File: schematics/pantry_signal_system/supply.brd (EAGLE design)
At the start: 71.1 x 61.3 mm, 58 parts, among them J1 USBASP_PIN, J2 JST-XH254-3P, J3 JST-XH254-2P, J4 JST-XH254-2P, Q1 FDS4935A, Q2 FDS4935A, Q3 FDS4935A, U1 NC7WZ04, U2 AD8544SO-14, U3 FAN73611, U4 FAN73611, U5 MCP1703T-5002E/CB, U6 MCP1703T-5002E/CB, U7 MCP1703T-3302E/CB, U8 FAN73611, U9 ATTINY13SO-8

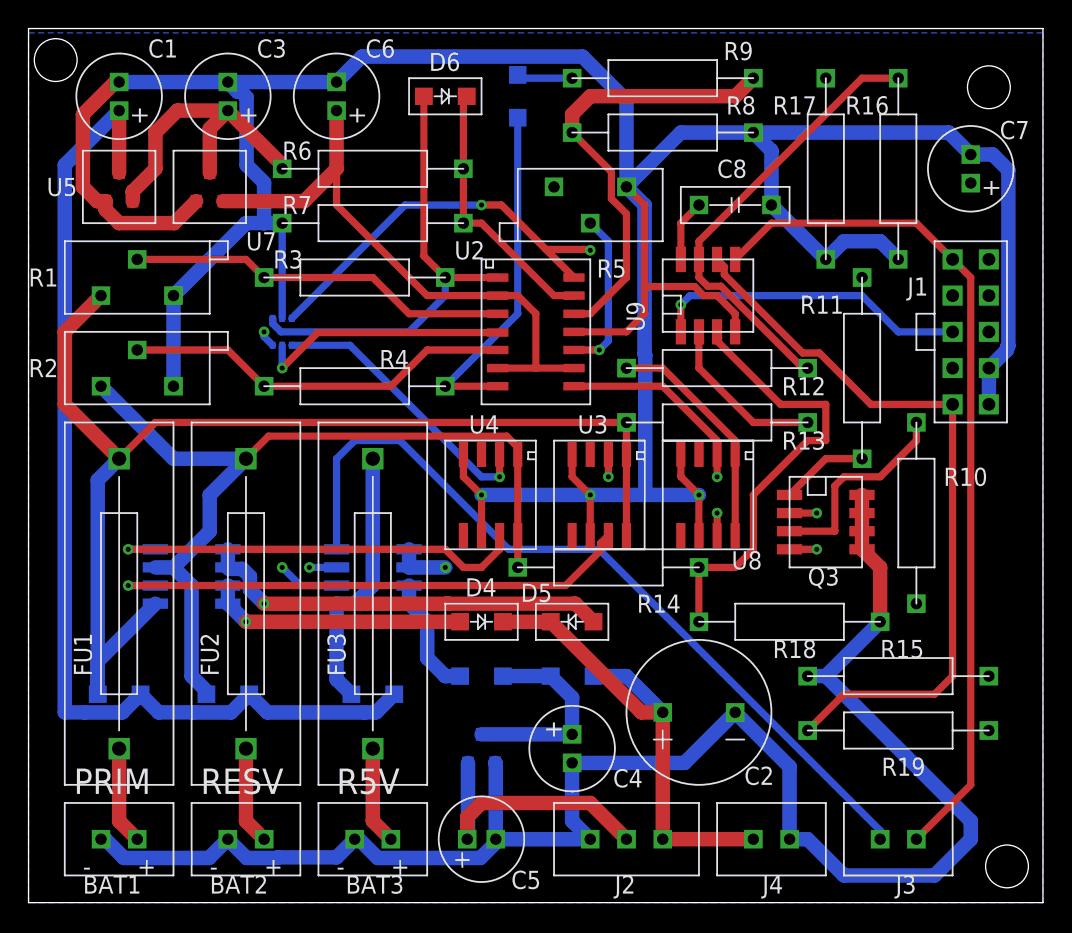
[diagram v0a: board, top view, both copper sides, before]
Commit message: Boards checked, some packages changed, library synced with this project
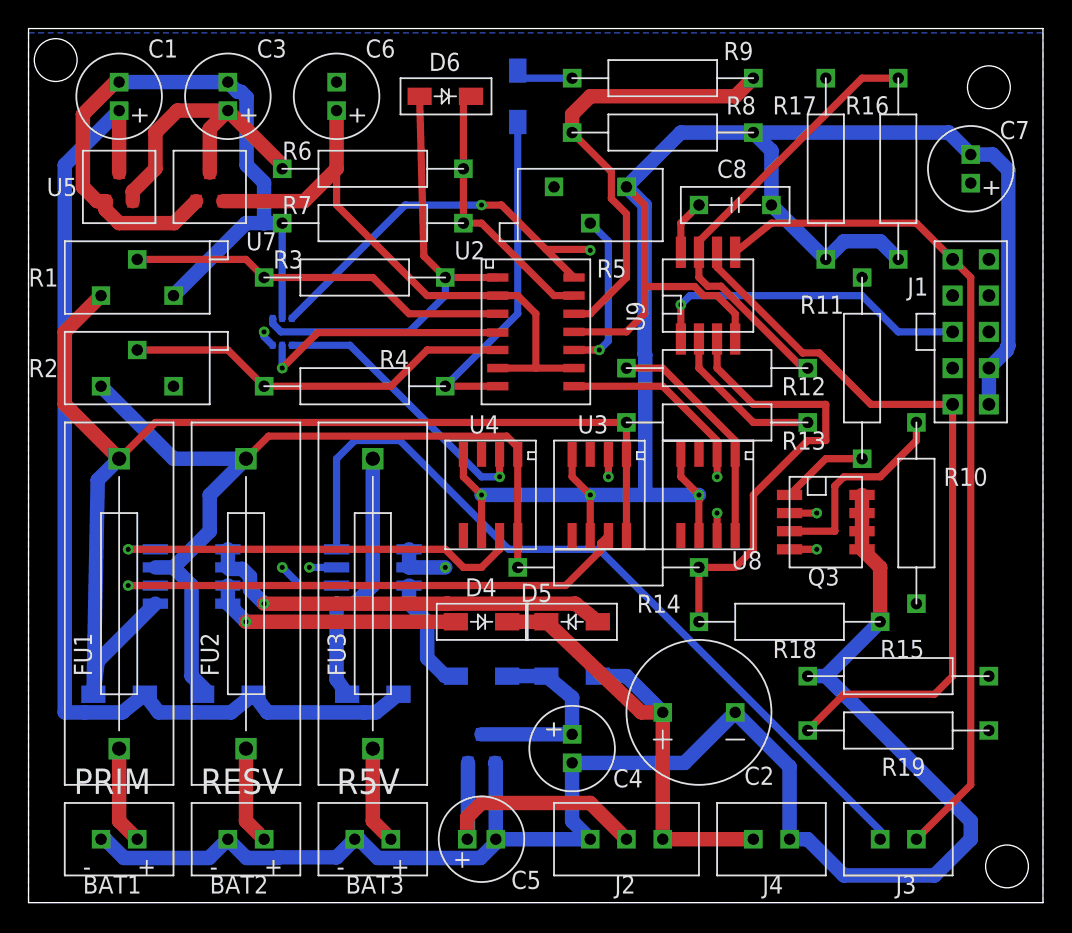
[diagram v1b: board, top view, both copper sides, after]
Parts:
- U9: value ATTINY13SO-8 -> ATTINY13SO-8-209; device my_devices:SO-8 -> my_devices:SO-8-209
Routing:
- net GND: track 412.5 -> 492.3 mm
- net +12V: track 75.0 -> 74.3 mm
- net RESERVE_VOLTAGE_LEVEL: track 31.3 -> 31.9 mm
- net SUPPLY_AVR_+5V: track 87.8 -> 87.3 mm
- net PRIMARY_VOLTAGE_LEVEL: track 38.5 -> 38.0 mm
- net N$17: track 22.3 -> 22.8 mm

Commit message: 1. Fixed issues in boards and firmwares
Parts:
- R1, R2, R5: device my_devices:RD-3296Z -> my_devices:RD-3296W-1-205LF
- moved R1 1.27 mm to (16.5, 58.4)
- moved R2 1.27 mm to (16.5, 52.1)
- moved R5 0.63 mm to (48.3, 64.1)
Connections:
- net +12V: now also J4.PIN2; no longer J4.PIN1
- net GND: now also J4.PIN1; no longer J4.PIN2
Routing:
- net +12V: track 74.3 -> 79.6 mm
- net GND: track 492.3 -> 496.9 mm
- net IS_12V_POWER_OK: track 11.5 -> 13.4 mm
- net N$1: track 74.1 -> 75.9 mm
- net SUPPLY_AVR_+5V: track 87.3 -> 88.6 mm
- net IS_USE_RESERVE_BATTERY: track 57.7 -> 59.0 mm
- net PRIMARY_SUPPLY_12V: track 83.8 -> 85.0 mm
- net N$3: track 26.8 -> 27.9 mm
- net N$9: track 31.5 -> 30.4 mm
- net SUPPLY_CONTROL_+5V: track 56.3 -> 56.8 mm
- net RESERVE_SUPPLY_12V: track 61.7 -> 62.2 mm
- net N$17: track 22.8 -> 22.2 mm

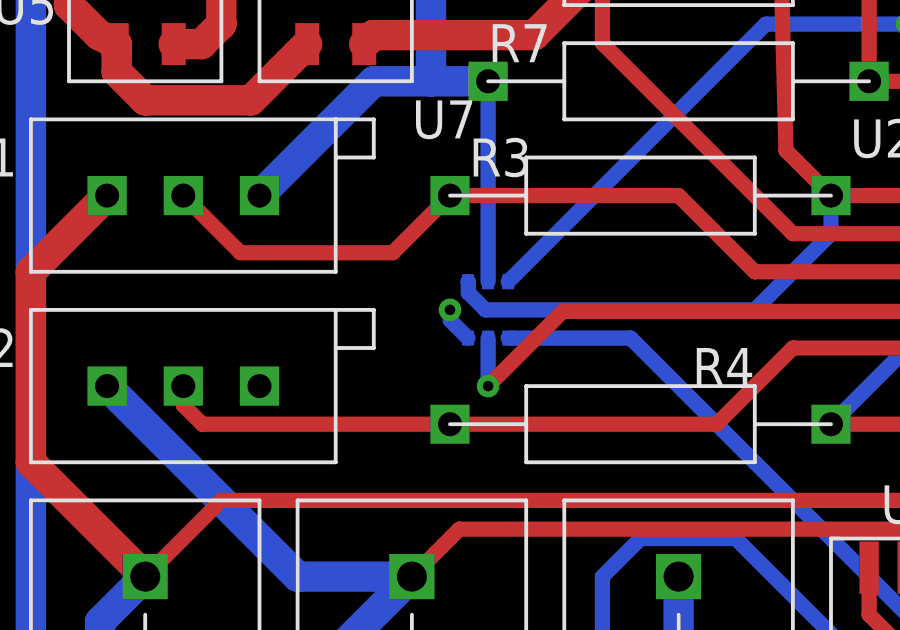
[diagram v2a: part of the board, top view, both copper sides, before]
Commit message: Changes in schematics, changes in source code. Current version works too, but I changed boards to fix some possible errors
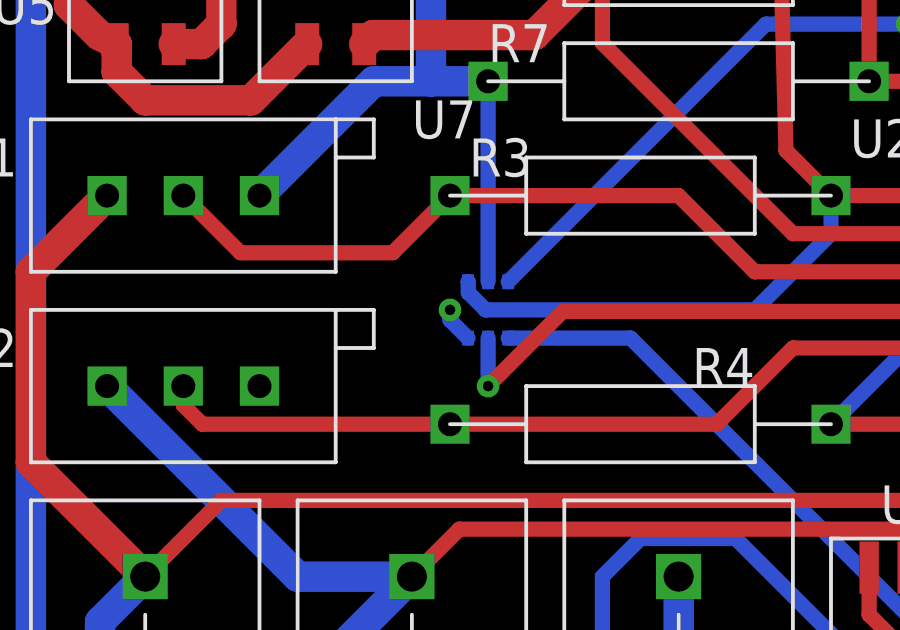
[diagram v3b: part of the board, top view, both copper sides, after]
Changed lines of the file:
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@@
 <contactref element="U3" pad="P_2"/>
 <wire x1="49.53" y1="46.02" x2="49.53" y2="44.45" width="0.508" layer="1"/>
-<wire x1="26" y1="53.67" x2="25.4" y2="54.27" width="0.508" layer="16"/>
 <via x="25.4" y="54.61" extent="1-16" drill="0.35"/>
 <via x="49.53" y="44.45" extent="1-16" drill="0.35"/>
 <wire x1="39.37" y1="54.61" x2="25.4" y2="54.61" width="0.508" layer="15"/>
 <wire x1="49.53" y1="44.45" x2="39.37" y2="54.61" width="0.508" layer="15"/>
-<wire x1="25.4" y1="54.61" x2="25.4" y2="54.27" width="0" layer="19" extent="16-16"/>
+<wire x1="26" y1="53.67" x2="25.4" y2="54.27" width="0.508" layer="16"/>
+<wire x1="25.4" y1="54.27" x2="25.4" y2="54.61" width="0.508" layer="16"/>
 </signal>
 <signal name="N$19">
